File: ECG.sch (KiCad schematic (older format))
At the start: 41 parts, among them J1 SJ-3566AN, J2 Conn_01x02_Male, Q1 MMBT3904-7-F, U1 ADR4525, U2 SP6641, U7 ADS1015IDGS

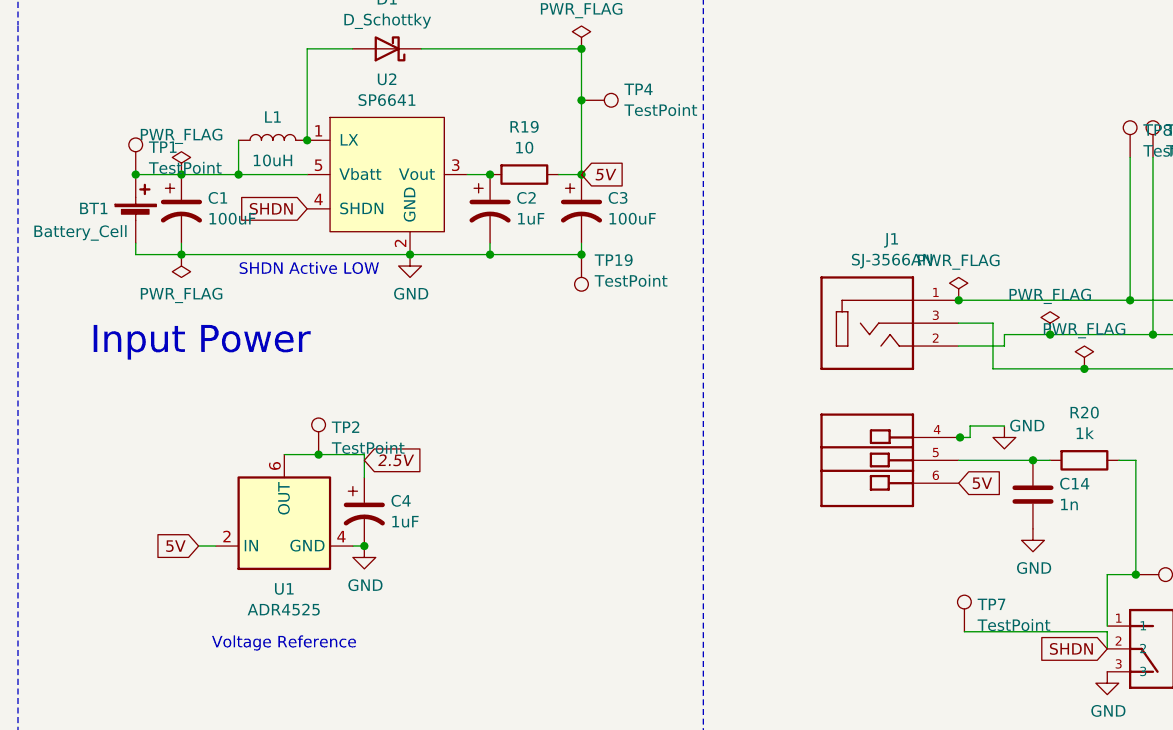
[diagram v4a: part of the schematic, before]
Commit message: Added bypass caps on ICs and fixed the SHDN input.
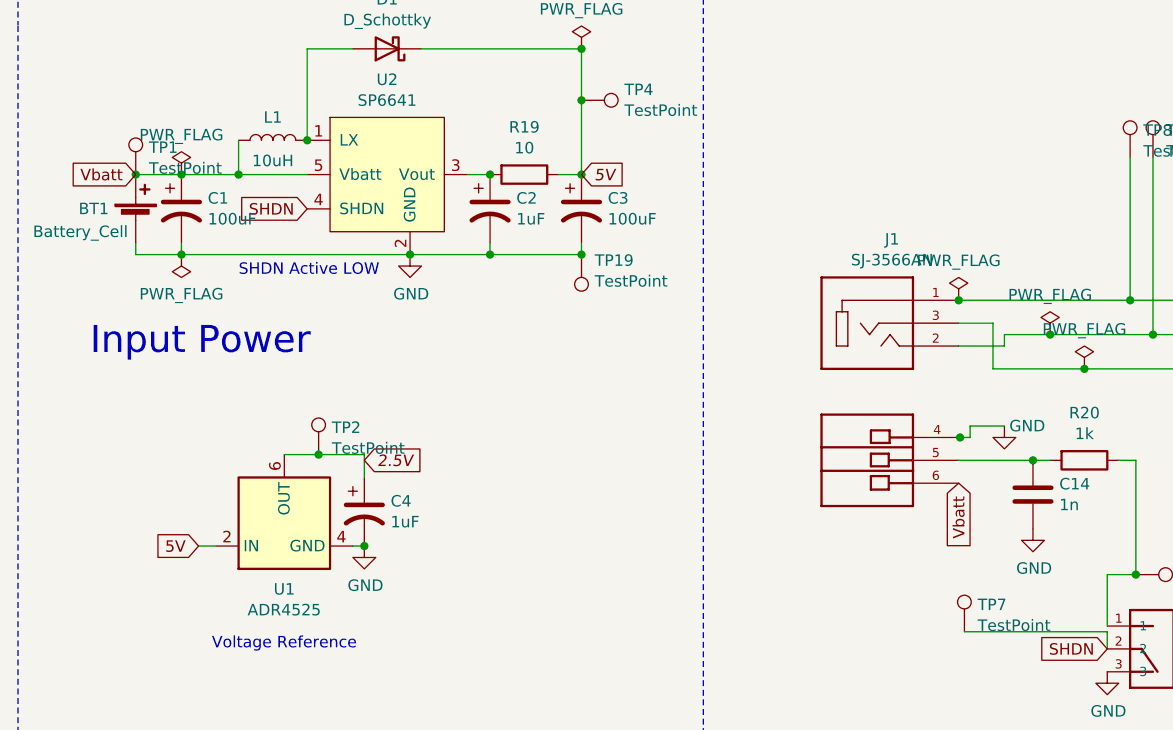
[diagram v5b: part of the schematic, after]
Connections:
- net labels added: Vbatt
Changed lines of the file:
@@
 Wire Wire Line
 	5775 3900 5700 3900
-Text GLabel 5000 4000 2    50   Input ~ 0
-5V
 $Comp
 L power:GND #PWR011
@@
 $EndComp
 Connection ~ 3350 3000
+Text GLabel 1400 2650 0    50   Input ~ 0
+Vbatt
+Text GLabel 5000 4000 3    50   Input ~ 0
+Vbatt
 $EndSCHEMATC

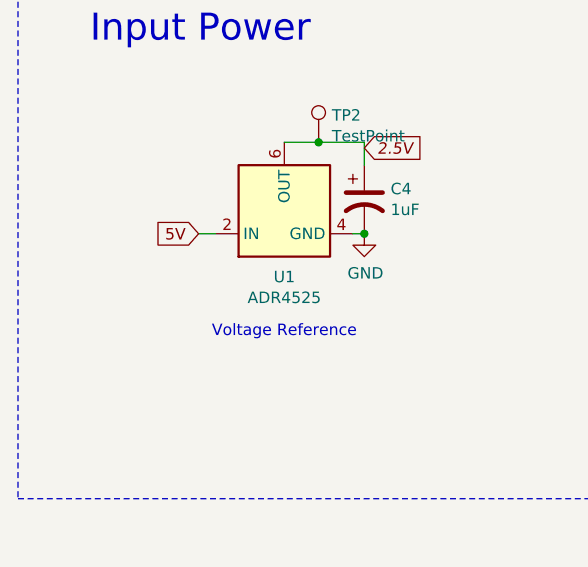
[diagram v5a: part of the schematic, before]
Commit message: Added bypass cap to Vref input
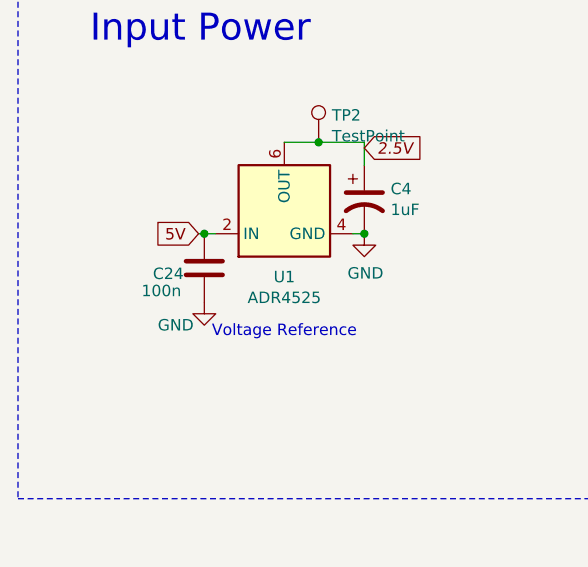
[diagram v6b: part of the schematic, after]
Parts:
- added C24: 100n, symbol Device:C
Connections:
- wire segments 78 -> 79
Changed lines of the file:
@@
 $EndComp
 Wire Wire Line
-	1750 4275 1675 4275
+	1750 4275 1700 4275
 Text GLabel 1675 4275 0    50   Input ~ 0
 5V
@@
 Text GLabel 5000 4000 3    50   Input ~ 0
 Vbatt
+$Comp
+L Device:C C24
+U 1 1 5FD00F60
+P 1700 4425
+F 0 "C24" H 1475 4400 50  0000 L CNN
+F 1 "100n" H 1425 4325 50  0000 L CNN
+F 2 "" H 1738 4275 50  0001 C CNN
+F 3 "~" H 1700 4425 50  0001 C CNN
+	1    1700 4425
+	1    0    0    -1
+$EndComp
+Connection ~ 1700 4275
+Wire Wire Line
+	1700 4275 1675 4275
+$Comp
+L power:GND #PWR025
+U 1 1 5FD01730
+P 1700 4575
+F 0 "#PWR025" H 1700 4325 50  0001 C CNN
+F 1 "GND" H 1575 4475 50  0000 C CNN
+F 2 "" H 1700 4575 50  0001 C CNN
+F 3 "" H 1700 4575 50  0001 C CNN
+	1    1700 4575
+	1    0    0    -1
+$EndComp
 $EndSCHEMATC

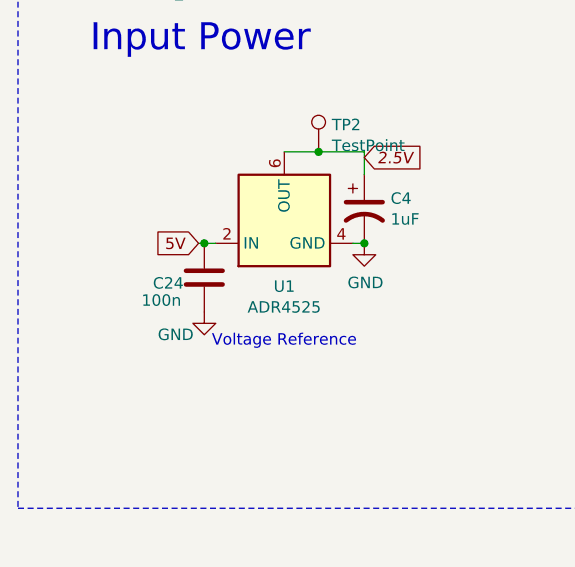
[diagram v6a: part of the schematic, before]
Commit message: Removed extra caps and removed the tantalum cap as it was too large
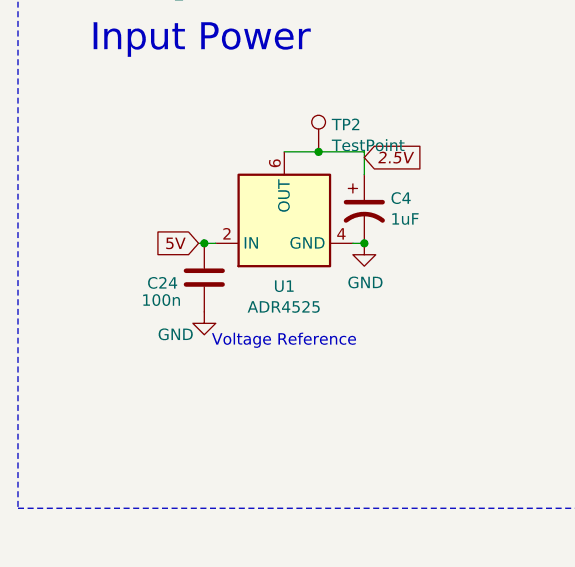
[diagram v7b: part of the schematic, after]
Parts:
- C24: footprint (none) -> Capacitor_SMD:C_0805_2012Metric_Pad1.18x1.45mm_HandSolder
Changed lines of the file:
@@
 U 1 1 5FD00F60
 P 1700 4425
-F 0 "C24" H 1475 4400 50  0000 L CNN
+F 0 "C24" H 1450 4400 50  0000 L CNN
 F 1 "100n" H 1425 4325 50  0000 L CNN
-F 2 "" H 1738 4275 50  0001 C CNN
+F 2 "Capacitor_SMD:C_0805_2012Metric_Pad1.18x1.45mm_HandSolder" H 1738 4275 50  0001 C CNN
 F 3 "~" H 1700 4425 50  0001 C CNN
 	1    1700 4425

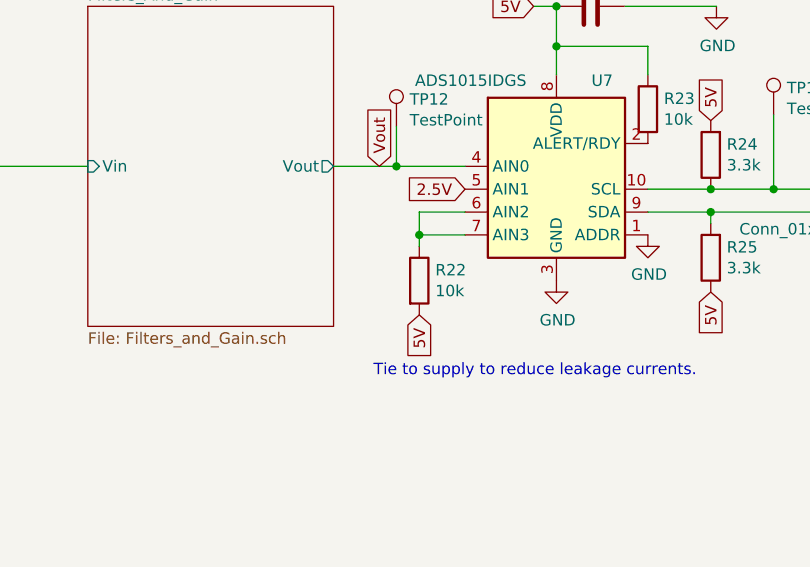
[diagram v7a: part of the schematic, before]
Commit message: Added battery voltage monitoring
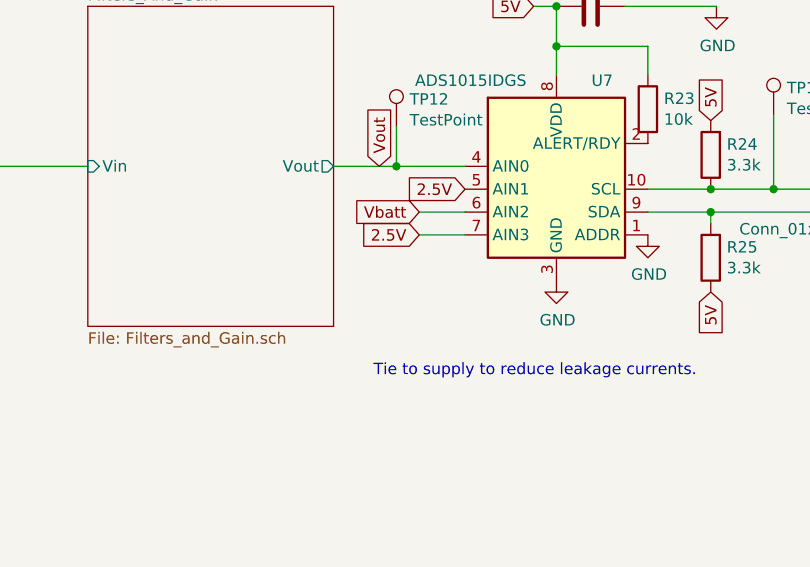
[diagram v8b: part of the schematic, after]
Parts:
- removed R22: 10k, Resistor_SMD:R_0805_2012Metric_Pad1.20x1.40mm_HandSolder, symbol Device:R
- J1: footprint CUI_SJ-3566AN -> Audio:CUI_SJ-3566AN
- S1: footprint SW_OS102011MS2QN1 -> Switches:SW_OS102011MS2QN1
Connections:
- wire segments 79 -> 77
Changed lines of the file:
@@
 F 0 "J1" H 4709 3667 50  0000 C CNN
 F 1 "SJ-3566AN" H 4709 3576 50  0000 C CNN
-F 2 "CUI_SJ-3566AN" H 4600 3300 50  0001 L BNN
+F 2 "Audio:CUI_SJ-3566AN" H 4600 3300 50  0001 L BNN
 F 3 "" H 4600 3300 50  0001 L BNN
 F 4 "Manufacturer recommendations" H 4600 3300 50  0001 L BNN "STANDARD"
@@
 F 0 "S1" H 5970 4771 50  0000 L CNN
 F 1 "OS102011MS2QN1" H 5970 4680 50  0000 L CNN
-F 2 "SW_OS102011MS2QN1" H 5850 4725 50  0001 L BNN
+F 2 "Switches:SW_OS102011MS2QN1" H 5850 4725 50  0001 L BNN
 F 3 "" H 5850 4725 50  0001 L BNN
 F 4 "C&K" H 5850 4725 50  0001 L BNN "MANUFACTURER"
@@
 Text GLabel 9225 3600 0    50   Input ~ 0
 2.5V
-$Comp
-L Device:R R22
-U 1 1 5FC0E4D1
-P 9025 4000
-F 0 "R22" H 9095 4046 50  0000 L CNN
-F 1 "10k" H 9095 3955 50  0000 L CNN
-F 2 "Resistor_SMD:R_0805_2012Metric_Pad1.20x1.40mm_HandSolder" V 8955 4000 50  0001 C CNN
-F 3 "~" H 9025 4000 50  0001 C CNN
-	1    9025 4000
-	1    0    0    -1
-$EndComp
 Wire Wire Line
 	9225 3700 9025 3700
 Wire Wire Line
 	9225 3800 9025 3800
-Wire Wire Line
-	9025 3700 9025 3800
-Connection ~ 9025 3800
-Wire Wire Line
-	9025 3800 9025 3850
-Text GLabel 9025 4150 3    50   Input ~ 0
-5V
 Text Notes 8825 4425 0    50   ~ 0
 Tie to supply to reduce leakage currents.
@@
 	1    0    0    -1
 $EndComp
+Text GLabel 9025 3700 0    50   Input ~ 0
+Vbatt
+Text GLabel 9025 3800 0    50   Input ~ 0
+2.5V
 $EndSCHEMATC
